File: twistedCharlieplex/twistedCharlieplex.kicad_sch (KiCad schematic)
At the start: 1 part, among them U2 STM32L412CBUxP

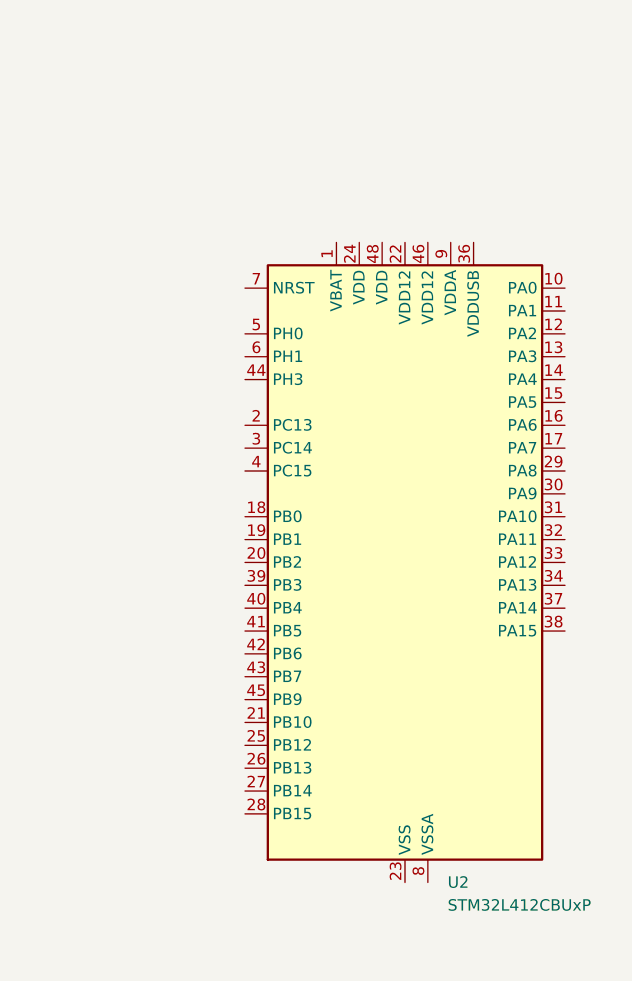
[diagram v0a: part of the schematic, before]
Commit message: Component layout locked. Trace nightmare time.
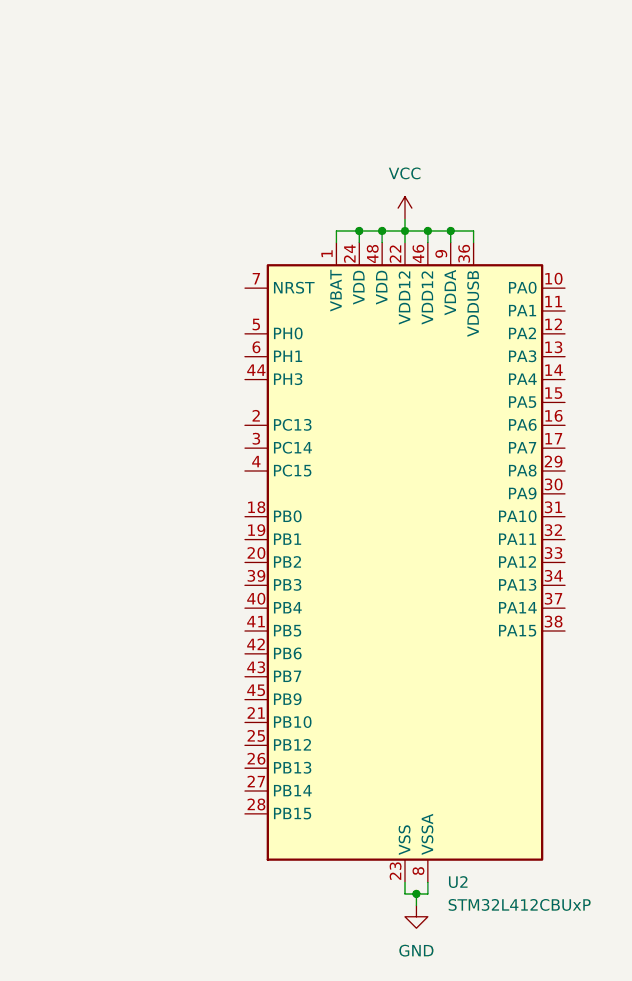
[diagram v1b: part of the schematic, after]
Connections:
- net VCC: now reaches U2.1 (VBAT)
- net VCC: now also U2.22 (VDD12), U2.24 (VDD), U2.36 (VDDUSB), U2.46 (VDD12), U2.48 (VDD), U2.9 (VDDA)
- net GND: now reaches U2.23 (VSS), U2.35 (VSS), U2.47 (VSS), U2.49 (VSS)
- net GND: now also U2.8 (VSSA)

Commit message: spirograph layout. let the nightmares begin
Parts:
- removed U2: STM32L412CBUxP, Package_DFN_QFN:QFN-48-1EP_7x7mm_P0.5mm_EP5.6x5.6mm, symbol MCU_ST_STM32L4:STM32L412CBUxP
- added AE1: Antenna_Shield, Antenna_SMD:C209892, symbol Device:Antenna_Shield
- added C1, C3: 100n, Capacitor_SMD:C_0402_1005Metric, symbol Device:C_Small
- added C2: 10u, Capacitor_SMD:C_0402_1005Metric, symbol Device:C_Small
- added C4, C5: 4p3, Capacitor_SMD:C_0402_1005Metric, symbol Device:C_Small
- added C6, C7: 12p, Capacitor_SMD:C_0402_1005Metric, symbol Device:C_Small
- added Q1: Q_PMOS_GSD, Package_TO_SOT_SMD:SOT-523, symbol Device:Q_PMOS_GSD
- added R1, R2, R3: 10k, Resistor_SMD:R_0402_1005Metric, symbol Device:R
- added R4: 100k, Resistor_SMD:R_0402_1005Metric, symbol Device:R_Small
- added R5: 1M, Resistor_SMD:R_0402_1005Metric, symbol Device:R_Small
- added U1: STM32L412CBUx, Package_DFN_QFN:QFN-48-1EP_7x7mm_P0.5mm_EP5.6x5.6mm, symbol MCU_ST_STM32L4:STM32L412CBUx
- added U2: LIS2DW12, Package_LGA:LGA-12_2x2mm_P0.5mm, symbol Sensor_IMU:LIS2DW12
- added U3: ESP32-C3, Package_DFN_QFN:QFN-32-1EP_5x5mm_P0.5mm_EP3.7x3.7mm, symbol MCU_Espressif:ESP32-C3
- added Y1: 32.768k, Crystal:Crystal_SMD_3215-2Pin_3.2x1.5mm, symbol Device:Crystal
- added Y2: 40M, SMD_Crystal:Crystal_SMD_1612_4P, symbol Device:Crystal_GND24_Small
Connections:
- net GND: now also AE1.2 (Shield), C1.2, C2.2, C3.1, C4.1, C5.1, C6.1, C7.1, R1.1, U1.23 (VSS), U1.35 (VSS), U1.47 (VSS), U1.49 (VSS), U1.8 (VSSA), U2.5 (NC), U2.6 (GND), U2.7 (RES), U2.8 (GND), U3.33 (GND), Y2.2, Y2.4
- new net: AE1.1 (A), U3.1 (LNA_IN)
- new net: C6.2, U3.29 (XTAL_N), Y2.3
- new net: C7.2, U3.30 (XTAL_P), Y2.1
- new net: R4.1, U3.7 (CHIP_EN)
- new net: C5.2, U1.4 (PC15), Y1.1
- new net: C4.2, U1.3 (PC14), Y1.2
- new net: C3.2, U1.7 (NRST)
- new net: R1.2, U1.44 (PH3)
- new net +3V0: C1.1, C2.1, Q1.2 (S), R2.2, R3.2, R5.2, U1.1 (VBAT), U1.24 (VDD), U1.48 (VDD), U1.9 (VDDA), U2.10 (VDD_IO), U2.9 (VDD)
- new net BOOT: U3.15 (GPIO9)
- new net ESP_PWR_EN: Q1.1 (G), R5.1, U1.28 (PB15)
- new net ESP_RX: U3.27 (U0RXD)
- new net ESP_TX: U3.28 (U0TXD)
- new net ESP_VDD: Q1.3 (D), R4.2, U3.11 (VDD3P3_RTC), U3.17 (VDD3P3_CPU), U3.18 (VDD_SPI), U3.2 (VDD3P3), U3.3 (VDD3P3), U3.31 (VDDA), U3.32 (VDDA)
- new net IO0: U1.11 (PA1)
- new net IO1: U1.12 (PA2)
- new net IO10: U1.31 (PA10)
- new net IO11: U1.32 (PA11)
- new net IO12: U1.33 (PA12)
- new net IO13: U1.38 (PA15)
- new net IO14: U1.18 (PB0)
- new net IO15: U1.19 (PB1)
- new net IO16: U1.39 (PB3)
- new net IO17: U1.40 (PB4)
- new net IO18: U1.41 (PB5)
- new net IO2: U1.13 (PA3)
- new net IO20: U1.45 (PB8)
- new net IO21: U1.46 (PB9)
- new net IO22: U1.21 (PB10)
- new net IO23: U1.22 (PB11)
- new net IO24: U1.25 (PB12)
- new net IO25: U1.26 (PB13)
- new net IO3: U1.14 (PA4)
- new net IO4: U1.15 (PA5)
- new net IO5: U1.16 (PA6)
- new net IO6: U1.17 (PA7)
- new net IO7: U1.29 (PA8)
- new net IO8: U1.30 (PA9)
- new net SCL: R2.1, U1.42 (PB6), U2.1 (SCL/SPC), U3.26 (GPIO19)
- new net SDA: R3.1, U1.43 (PB7), U2.4 (SDA/SDI/SDO), U3.25 (GPIO18)
- new net SWDIO: U1.34 (PA13)
- new net SWSCK: U1.37 (PA14)
- new net WKUP1: U1.10 (PA0), U2.12 (INT1)
- no-connect marks 0 -> 21
